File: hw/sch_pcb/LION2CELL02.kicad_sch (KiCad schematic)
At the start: 11 parts

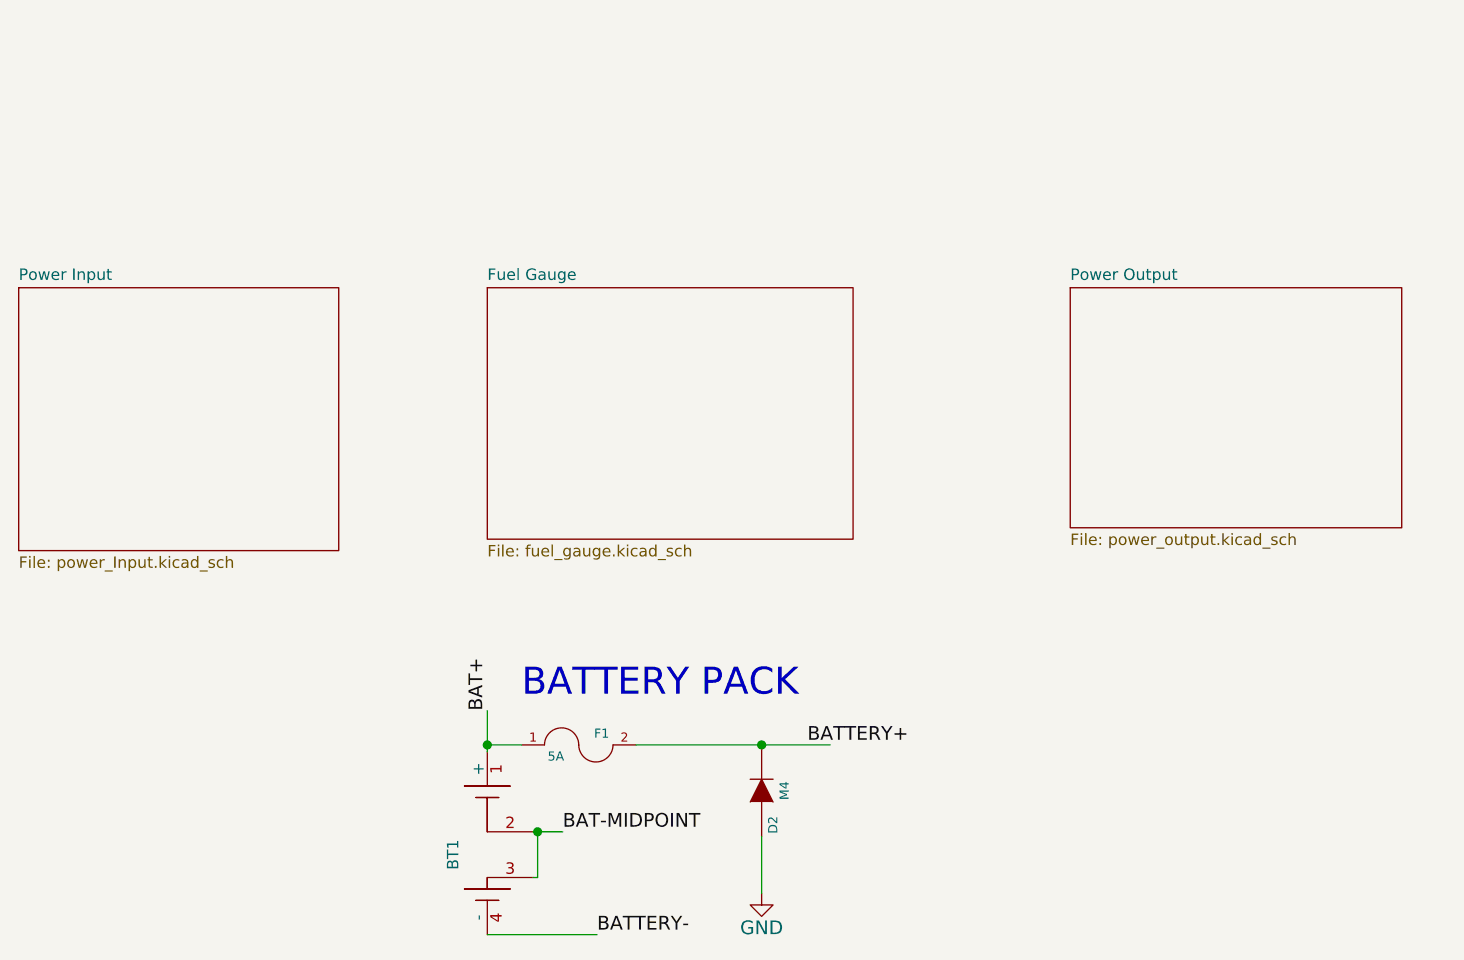
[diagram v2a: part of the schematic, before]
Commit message: Schematics work. PCB layout initial schematics import.
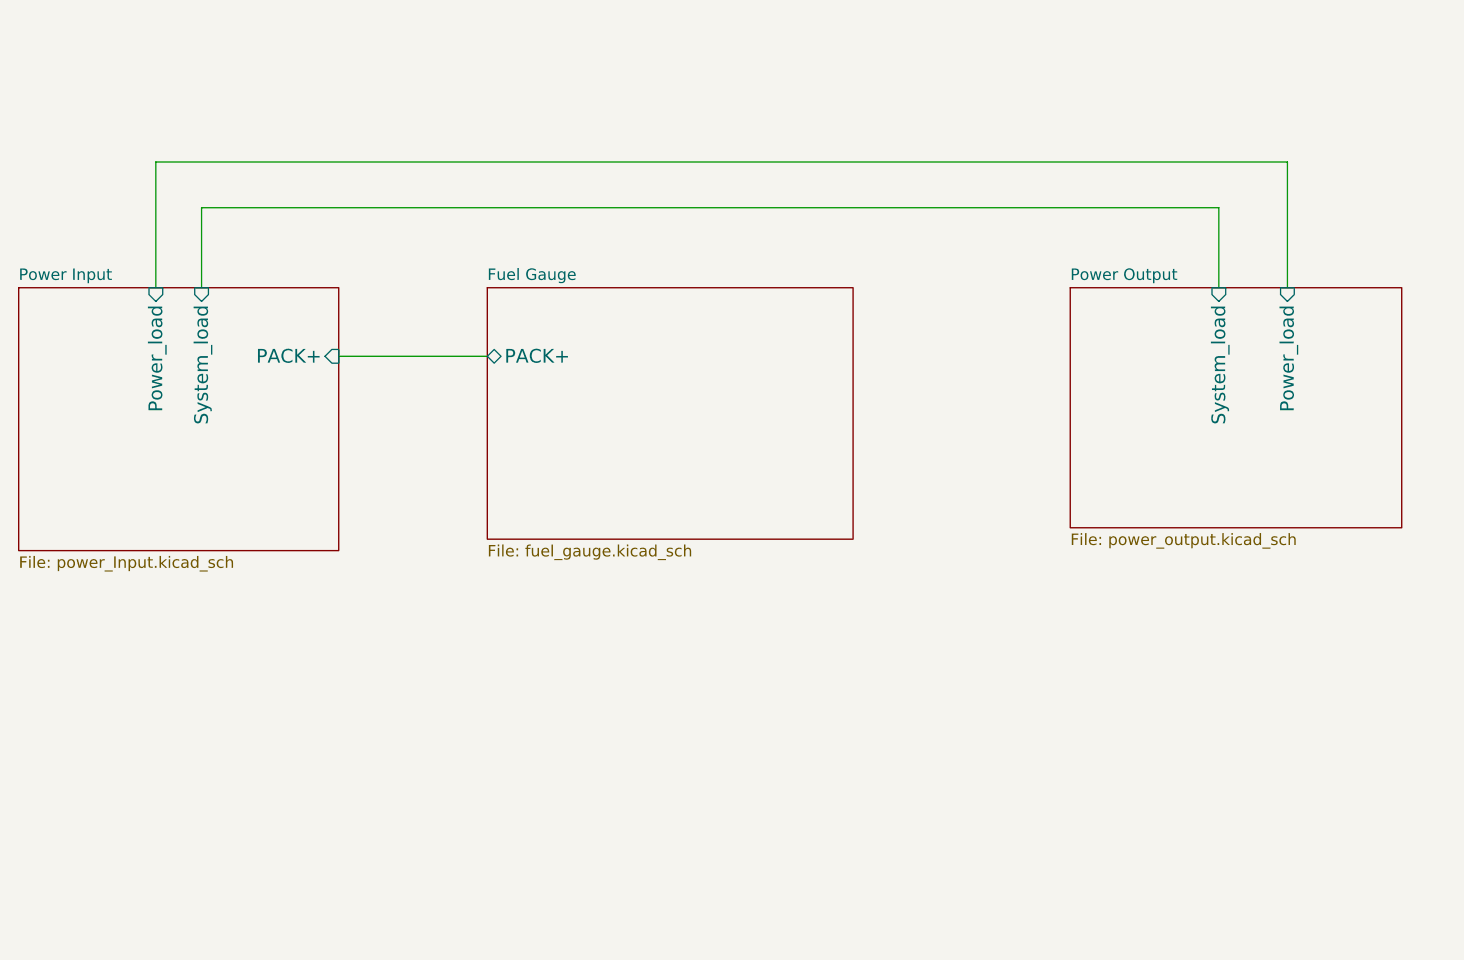
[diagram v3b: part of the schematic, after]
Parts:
- removed BT1: 2x18650_LION-RESCUE-LION2CELL01C, Mlab_Batery:2LION, symbol LION2CELL01D-rescue:2x18650_LION-RESCUE-LION2CELL01C
- removed D2: M4, Mlab_D:SMA_Standard, symbol LION2CELL01D-rescue:DIODE
- removed F1: 5A, Mlab_F:Drzak_2410, symbol LION2CELL01D-rescue:FUSE
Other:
- sheet Fuel Gauge ports: added PACK+; removed none
- sheet Power Input ports: added PACK+, Power_load, System_load; removed none
- sheet Power Output ports: added Power_load, System_load; removed none
- note removed: "BATTERY PACK"

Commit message: Partially routed PCB.
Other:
- sheet Fuel Gauge ports: added SCL, SDA; removed none
- sheet Power Input ports: added SCL, SDA; removed none
- sheet Power Output ports: added SCL, SDA; removed none
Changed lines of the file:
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@@
 		(color 0 0 0 0)
 	)
+	(junction
+		(at 163.83 101.6)
+		(diameter 0)
+		(color 0 0 0 0)
+	)
+	(junction
+		(at 166.37 100.33)
+		(diameter 0)
+		(color 0 0 0 0)
+	)
+	(wire
+		(pts
+			(xy 163.83 92.71) (xy 163.83 101.6)
+		)
+		(stroke
+			(width 0)
+			(type default)
+		)
+	)
 	(wire
 		(pts
@@
 	(wire
 		(pts
+			(xy 106.68 101.6) (xy 163.83 101.6)
+		)
+		(stroke
+			(width 0)
+			(type default)
+		)
+	)
+	(wire
+		(pts
+			(xy 228.6 91.44) (xy 228.6 100.33)
+		)
+		(stroke
+			(width 0)
+			(type default)
+		)
+	)
+	(wire
+		(pts
+			(xy 166.37 100.33) (xy 228.6 100.33)
+		)
+		(stroke
+			(width 0)
+			(type default)
+		)
+	)
+	(wire
+		(pts
 			(xy 218.44 50.8) (xy 218.44 64.77)
 		)
@@
 	(wire
 		(pts
+			(xy 109.22 100.33) (xy 109.22 93.98)
+		)
+		(stroke
+			(width 0)
+			(type default)
+		)
+	)
+	(wire
+		(pts
 			(xy 210.82 64.77) (xy 210.82 55.88)
 		)
@@
 	(wire
 		(pts
+			(xy 109.22 100.33) (xy 166.37 100.33)
+		)
+		(stroke
+			(width 0)
+			(type default)
+		)
+	)
+	(wire
+		(pts
 			(xy 260.35 29.21) (xy 260.35 30.48)
 		)
@@
 			(width 0)
 			(type solid)
+		)
+	)
+	(wire
+		(pts
+			(xy 106.68 93.98) (xy 106.68 101.6)
+		)
+		(stroke
+			(width 0)
+			(type default)
+		)
+	)
+	(wire
+		(pts
+			(xy 163.83 101.6) (xy 226.06 101.6)
+		)
+		(stroke
+			(width 0)
+			(type default)
+		)
+	)
+	(wire
+		(pts
+			(xy 226.06 101.6) (xy 226.06 91.44)
+		)
+		(stroke
+			(width 0)
+			(type default)
+		)
+	)
+	(wire
+		(pts
+			(xy 166.37 92.71) (xy 166.37 100.33)
+		)
+		(stroke
+			(width 0)
+			(type default)
 		)
 	)
@@
 			)
 		)
+		(pin "SDA" input
+			(at 109.22 93.98 270)
+			(effects
+				(font
+					(size 1.524 1.524)
+				)
+				(justify left)
+			)
+		)
+		(pin "SCL" input
+			(at 106.68 93.98 270)
+			(effects
+				(font
+					(size 1.524 1.524)
+				)
+				(justify left)
+			)
+		)
 		(instances
 			(project "LION2CELL02"
@@
 			)
 		)
+		(pin "SDA" input
+			(at 228.6 91.44 270)
+			(effects
+				(font
+					(size 1.524 1.524)
+				)
+				(justify left)
+			)
+		)
+		(pin "SCL" input
+			(at 226.06 91.44 270)
+			(effects
+				(font
+					(size 1.524 1.524)
+				)
+				(justify left)
+			)
+		)
 		(instances
 			(project "LION2CELL02"
@@
 			(effects
 				(font
+					(size 1.524 1.524)
+				)
+				(justify left)
+			)
+		)
+		(pin "SCL" input
+			(at 163.83 92.71 270)
+			(effects
+				(font
+					(size 1.524 1.524)
+				)
+				(justify left)
+			)
+		)
+		(pin "SDA" input
+			(at 166.37 92.71 270)
+			(effects
+				(font

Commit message: Adding output voltage switching regulator.
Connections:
- removed net GND: H1.1, H2.1, H3.1, H4.1
- no-connect marks 0 -> 4
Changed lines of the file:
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@@
-	)
-	(junction
-		(at 264.16 29.21)
-		(diameter 1.016)
-		(color 0 0 0 0)
-	)
-	(junction
-		(at 260.35 29.21)
-		(diameter 1.016)
-		(color 0 0 0 0)
-	)
-	(junction
-		(at 255.27 29.21)
-		(diameter 1.016)
-		(color 0 0 0 0)
 	)
 	(junction
@@
 		(color 0 0 0 0)
 	)
+	(no_connect
+		(at 246.38 27.94)
+	)
+	(no_connect
+		(at 271.78 27.94)
+	)
+	(no_connect
+		(at 264.16 27.94)
+	)
+	(no_connect
+		(at 255.27 27.94)
+	)
 	(wire
 		(pts
@@
 	(wire
 		(pts
-			(xy 246.38 27.94) (xy 246.38 29.21)
-		)
-		(stroke
-			(width 0)
-			(type solid)
-		)
-	)
-	(wire
-		(pts
 			(xy 97.79 55.88) (xy 97.79 64.77)
 		)
@@
 	(wire
 		(pts
-			(xy 246.38 29.21) (xy 255.27 29.21)
-		)
-		(stroke
-			(width 0)
-			(type solid)
-		)
-	)
-	(wire
-		(pts
 			(xy 92.71 64.77) (xy 92.71 50.8)
 		)
@@
 	(wire
 		(pts
-			(xy 264.16 27.94) (xy 264.16 29.21)
-		)
-		(stroke
-			(width 0)
-			(type solid)
-		)
-	)
-	(wire
-		(pts
-			(xy 271.78 29.21) (xy 271.78 27.94)
-		)
-		(stroke
-			(width 0)
-			(type solid)
-		)
-	)
-	(wire
-		(pts
-			(xy 260.35 29.21) (xy 264.16 29.21)
-		)
-		(stroke
-			(width 0)
-			(type solid)
-		)
-	)
-	(wire
-		(pts
 			(xy 109.22 100.33) (xy 109.22 93.98)
 		)
@@
 	(wire
 		(pts
-			(xy 264.16 29.21) (xy 271.78 29.21)
-		)
-		(stroke
-			(width 0)
-			(type solid)
-		)
-	)
-	(wire
-		(pts
 			(xy 109.22 100.33) (xy 166.37 100.33)
 		)
@@
 	(wire
 		(pts
-			(xy 260.35 29.21) (xy 260.35 30.48)
-		)
-		(stroke
-			(width 0)
-			(type solid)
-		)
-	)
-	(wire
-		(pts
-			(xy 255.27 29.21) (xy 260.35 29.21)
-		)
-		(stroke
-			(width 0)
-			(type solid)
-		)
-	)
-	(wire
-		(pts
 			(xy 106.68 93.98) (xy 106.68 101.6)
 		)
@@
 			(width 0)
 			(type default)
-		)
-	)
-	(wire
-		(pts
-			(xy 255.27 27.94) (xy 255.27 29.21)
-		)
-		(stroke
-			(width 0)
-			(type solid)
 		)
 	)
@@
 					(unit 1)
 				)
-			)
-		)
-	)
-	(symbol
-		(lib_id "power:GND")
-		(at 260.35 30.48 0)
-		(unit 1)
-		(exclude_from_sim no)
-		(in_bom yes)
-		(on_board yes)
-		(dnp no)
-		(property "Reference" "#PWR08"
-			(at 260.35 36.83 0)
-			(effects
-				(font
-					(size 1 1)
-				)
-				(hide yes)
-			)
-		)
-		(property "Value" "GND"
-			(at 264.16 31.75 0)
-			(effects
-				(font
-					(size 1 1)
-				)
-			)
-		)
-		(property "Footprint" ""
-			(at 260.35 30.48 0)
-			(effects
-				(font
-					(size 1 1)
-				)
-				(hide yes)
-			)
-		)
-		(property "Datasheet" ""
-			(at 260.35 30.48 0)
-			(effects
-				(font
-					(size 1 1)
-				)
-				(hide yes)
-			)
-		)
-		(property "Description" ""
-			(at 260.35 30.48 0)
-			(effects
-				(font
-					(size 1.27 1.27)
-				)
-				(hide yes)
-			)
-		)
-		(pin "1"
-		)
-		(instances
-			(project "LION2CELL02"
-				(path "/cf3ec207-cc3b-4c92-9c2d-71c8a9dee6d9"
-					(reference "#PWR08")
-					(unit 1)
-				)
